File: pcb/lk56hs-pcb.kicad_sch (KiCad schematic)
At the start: 8 parts, among them J2 Conn_01x03, U1 RaspberryPi_Pico

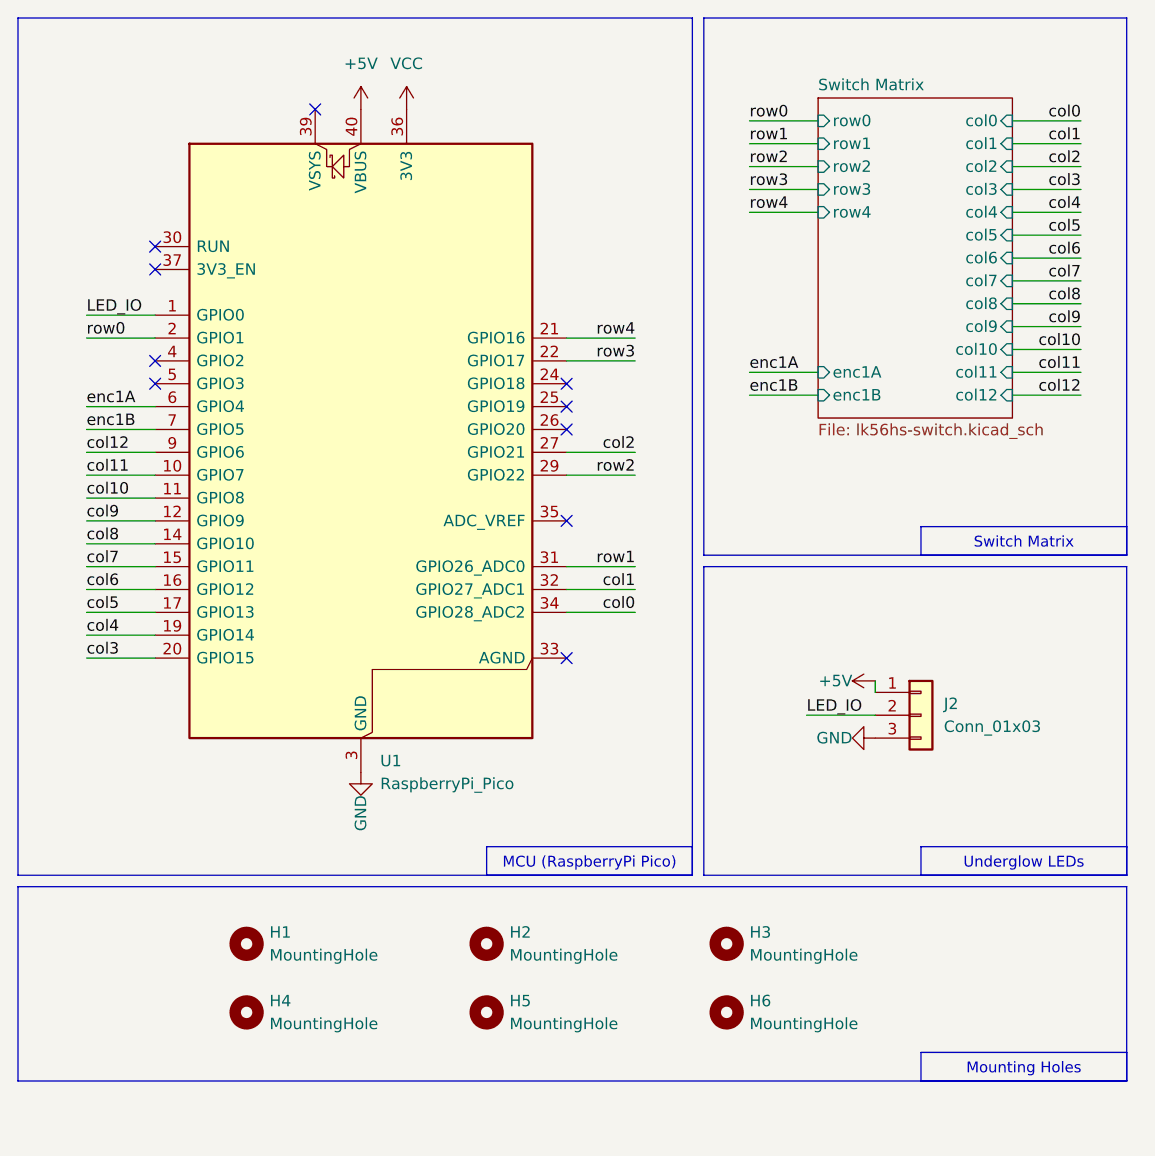
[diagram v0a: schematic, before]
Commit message: Add simple plate
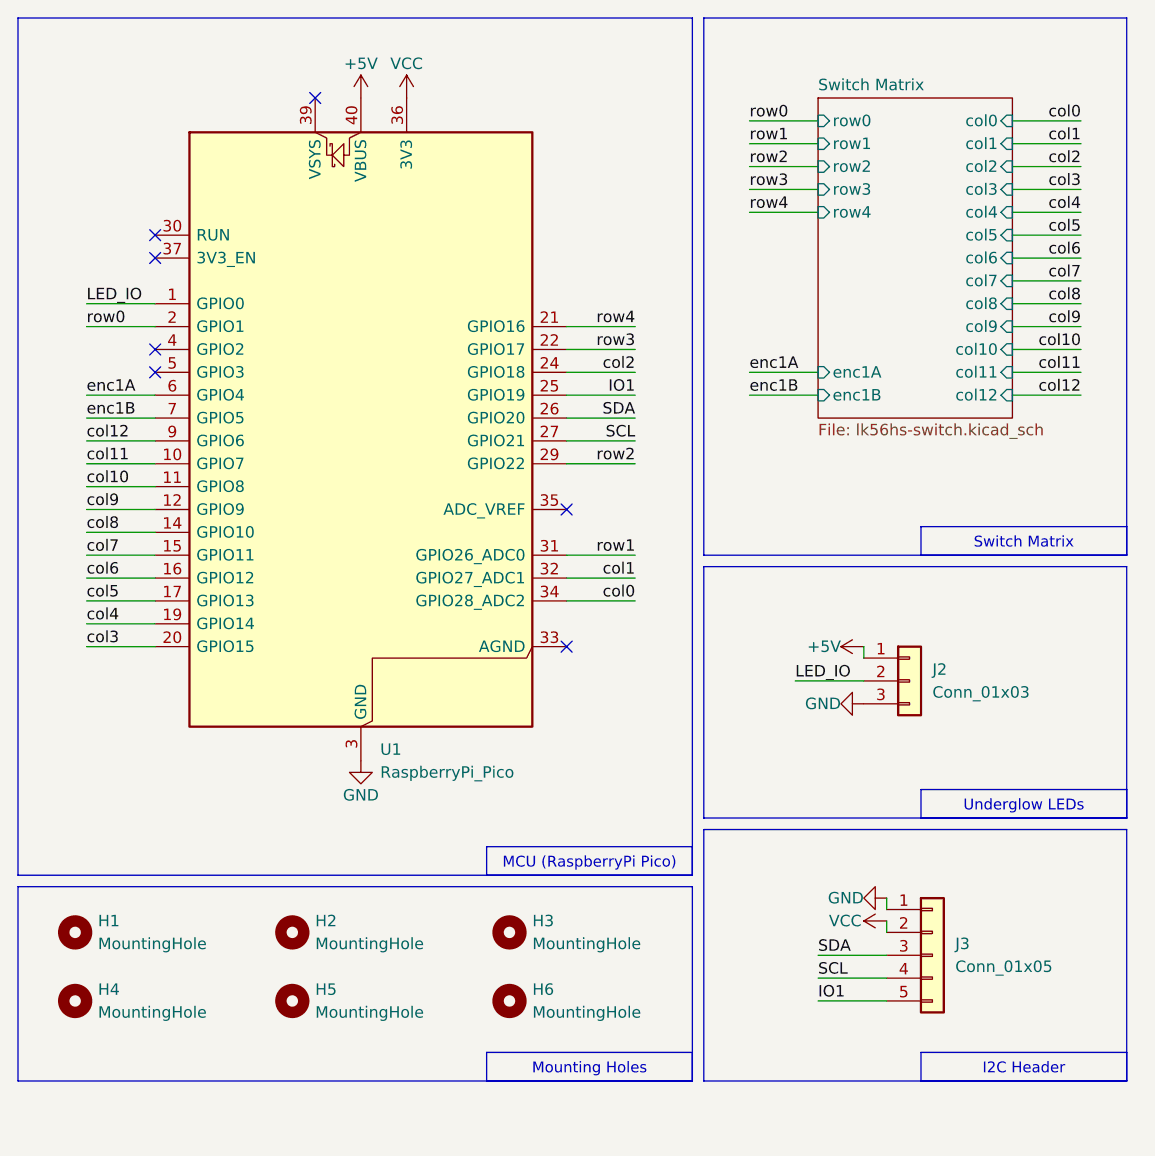
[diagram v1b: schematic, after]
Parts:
- added J3: Conn_01x05, LKBD_Connector:PinHeader_1x05_THT_P2.54mm_nSilk, symbol Connector_Generic:Conn_01x05
- H3, H4, H6: footprint LKBD_MountingHole:MountingHole_M2_Oval_NPTH -> LKBD_MountingHole:MountingSlot_M2_Small_NPTH
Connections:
- net GND: now also J3.1 (Pin_1)
- net VCC: now also J3.2 (Pin_2)
- net col2: now also U1.24 (GPIO18); no longer U1.27 (GPIO21)
- net IO1: now reaches U1.25 (GPIO19)
- net IO1: now also J3.5 (Pin_5)
- net SDA: now reaches U1.26 (GPIO20)
- net SDA: now also J3.3 (Pin_3)
- new net SCL: J3.4 (Pin_4), U1.27 (GPIO21)
- no-connect marks 10 -> 7
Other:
- note added: "I2C Header"
- moved on the sheet: H1, H2, H3, H4, H5, H6, J2, U1

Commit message: Make plate reversible and add graphics
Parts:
- added H7, H8: MountingHole, LKBD_MountingHole:MountingHole_M2_NoPad, symbol Mechanical:MountingHole
- H1: footprint LKBD_MountingHole:MountingHole_M2_NPTH -> LKBD_MountingHole:MountingHole_M2_NoPad
- H2: renamed from H3; footprint LKBD_MountingHole:MountingSlot_M2_Small_NPTH -> LKBD_MountingHole:MountingHole_M2_NoPad
- H3: renamed from H2; footprint LKBD_MountingHole:MountingSlot_M2_NTPH_Half -> LKBD_MountingHole:MountingHole_M2_NoPad
- H4, H6: footprint LKBD_MountingHole:MountingSlot_M2_Small_NPTH -> LKBD_MountingHole:MountingHole_M2_NoPad
- H5: footprint LKBD_MountingHole:MountingSlot_M2_NTPH_Long -> LKBD_MountingHole:MountingHole_M2_NoPad
- J2: value Conn_01x03 -> PINHD_1x03_ARGB; symbol Connector_Generic:Conn_01x03 -> LKBD_Connector:PINHD_1x03_ARGB
- J3: value Conn_01x05 -> PINHD_1x05_I2C; symbol Connector_Generic:Conn_01x05 -> LKBD_Connector:PINHD_1x05_I2C
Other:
- moved on the sheet: H3, H5
